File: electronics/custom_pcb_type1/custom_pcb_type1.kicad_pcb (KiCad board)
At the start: 2 copper layers, 124.5 x 81.3 mm, 25 parts, among them J1 BELT_CONN_1, J2 BELT_CONN_2, J3 SEN0140, J4 USB_B, J5 JMPR_TO_ATMEGA, Q1 2N2222, Q2 2N2222, Q3 2N2222, Q4 2N2222, Q5 2N2222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

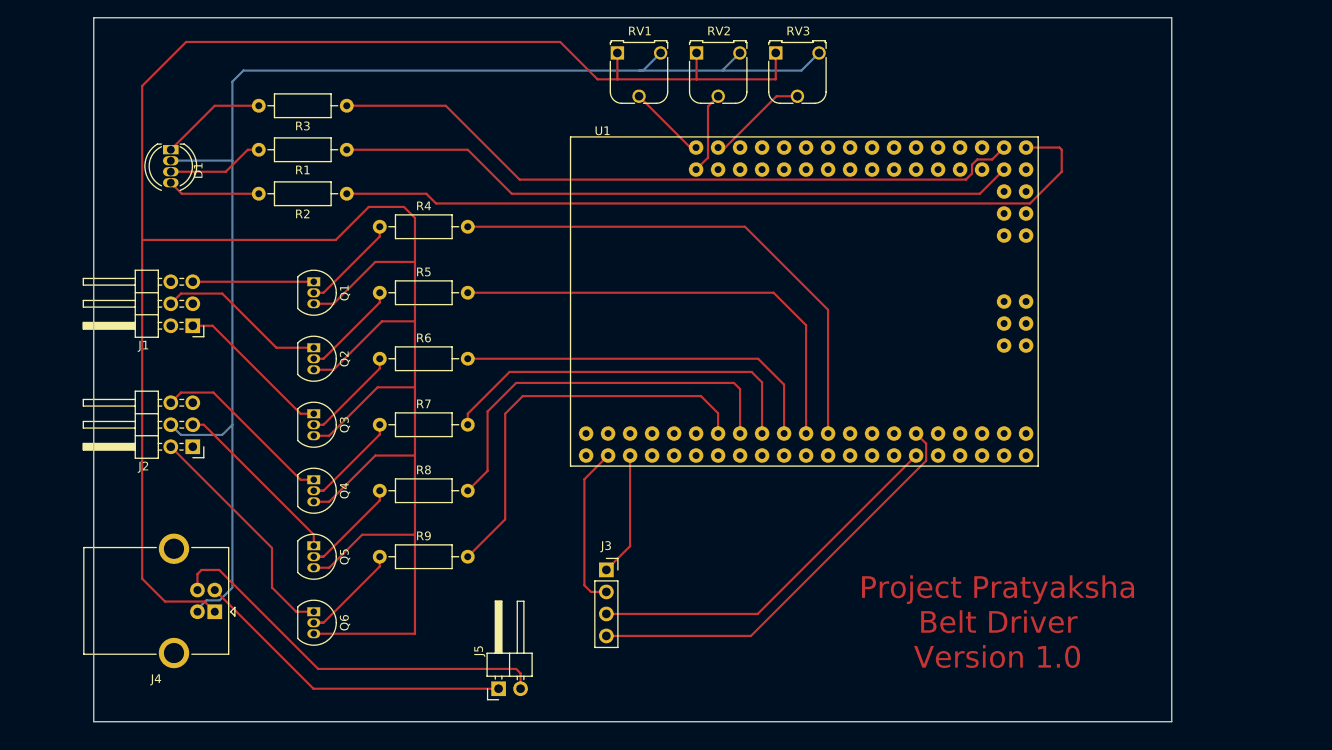
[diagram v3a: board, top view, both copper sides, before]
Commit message: Size matters
Welp Got all the way to putting the transfer paper onto the PCB when I found out that my raw PCBs are kinda small. 70mm x 100mm - which is a lot smaller than the current footprint of like 90mm x 120mm. So LOTS of rearranging things and reassigning pins. I think the end result is a far better board than the previous one so It was well worth the effort. I made sure to not route any traces too close to the edge, other traces, or other pin holes. Trying to give the toner transfer the best possible chance of at least not bridging stuff.
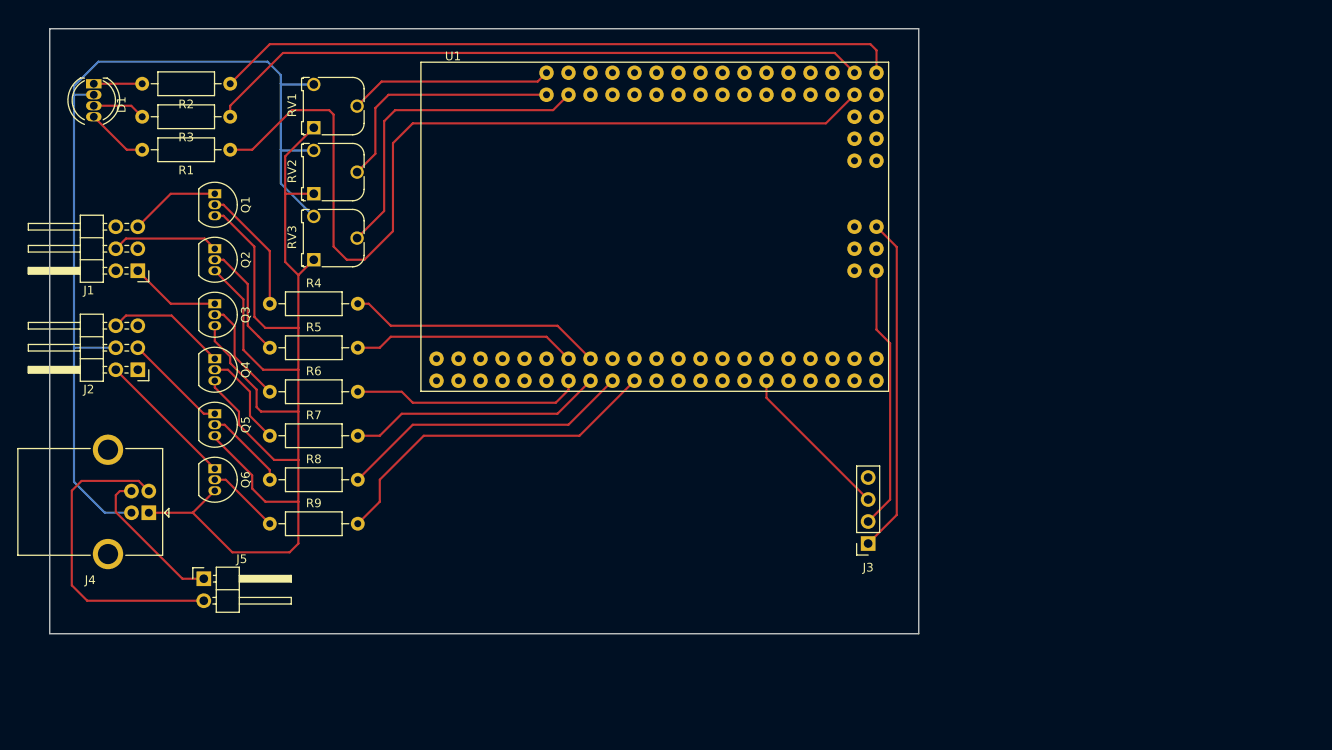
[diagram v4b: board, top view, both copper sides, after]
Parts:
- moved RV3 58.4 mm to (94.0, 94.0), turned to 90 degrees
- moved RV2 47.1 mm to (94.0, 86.4), turned to 90 degrees
- moved J5 36.3 mm to (81.3, 130.8), turned to 0 degrees
- moved RV1 36.1 mm to (94.0, 78.7), turned to 90 degrees
- moved J3 30.4 mm to (158.0, 126.7), turned to 180 degrees
- moved Q6 20.1 mm to (82.5, 118.1)
- moved U1 19.3 mm to (133.3, 90.2)
- moved Q5 19.1 mm to (82.5, 111.8)
- moved R2 18.5 mm to (84.3, 73.7)
- moved Q4 18.1 mm to (82.5, 105.4)
- moved Q3 17.1 mm to (82.5, 99.1)
- moved Q2 16.2 mm to (82.5, 92.7)
- moved R4 15.5 mm to (88.9, 99.1)
- moved Q1 15.3 mm to (82.5, 86.4)
- moved R5 14.2 mm to (88.9, 104.1)
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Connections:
- J5 pad 1: Net-(J4-Pad2) -> Net-(J4-Pad3)
- J5 pad 2: Net-(J4-Pad3) -> Net-(J4-Pad2)
- R1 pad 2: Net-(D1-Pad3) -> Net-(D1-Pad4)
- R2 pad 2: Net-(D1-Pad4) -> Net-(D1-Pad1)
- R3 pad 2: Net-(D1-Pad1) -> Net-(D1-Pad3)
- U1 pad A2: Net-(RV3-Pad2) -> Net-(U1-PadA2)
- U1 pad A3: Net-(U1-PadA3) -> Net-(RV3-Pad2)
- U1 pad D10: Net-(R5-Pad2) -> Net-(U1-PadD10)
- U1 pad D12: Net-(R4-Pad2) -> Net-(U1-PadD12)
- U1 pad D2: Net-(R9-Pad2) -> Net-(R5-Pad2)
- U1 pad D3: Net-(U1-PadD3) -> Net-(R6-Pad2)
- U1 pad D4: Net-(R8-Pad2) -> Net-(R4-Pad2)
- U1 pad D5: Net-(U1-PadD5) -> Net-(R7-Pad2)
- U1 pad D6: Net-(R7-Pad2) -> Net-(U1-PadD6)
- U1 pad D7: Net-(U1-PadD7) -> Net-(R8-Pad2)
- U1 pad D8: Net-(R6-Pad2) -> Net-(U1-PadD8)
- U1 pad D9: Net-(U1-PadD9) -> Net-(R9-Pad2)
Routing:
- net +5V: track 315.2 -> 161.6 mm
- net Net-(J3-Pad4): track 48.9 -> 0.00 mm
- net GND: track 154.2 -> 112.2 mm
- net Net-(R4-Pad2): track 59.9 -> 29.5 mm
- net Net-(J4-Pad3): track 46.1 -> 17.3 mm
- net Net-(R5-Pad2): track 53.1 -> 25.9 mm
- net Net-(RV3-Pad2): track 11.6 -> 37.3 mm
- net Net-(J3-Pad3): track 43.3 -> 18.6 mm
- net Net-(R1-Pad1): track 79.2 -> 103.9 mm
- net Net-(J3-Pad1): track 15.2 -> 38.9 mm
- net Net-(RV2-Pad2): track 9.52 -> 28.7 mm
- net Net-(R6-Pad2): track 43.4 -> 26.5 mm
- net Net-(RV1-Pad2): track 9.04 -> 23.5 mm
- net Net-(R7-Pad2): track 43.7 -> 29.5 mm
- net Net-(R8-Pad2): track 46.0 -> 34.1 mm
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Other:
- board size 124.5 x 81.3 mm -> 100.3 x 69.8 mm
- board text removed: "Project Pratyaksha Belt Driver Version 1.0"

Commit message: Forgot some text
Forgot the text I added to identify the board and version. It should be nicely visible even after all components are on the board.
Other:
- board text added: "Project Pratyaksha Belt Driver Version 1.0"
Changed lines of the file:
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@@
   (general
     (thickness 1.6)
-    (drawings 9)
+    (drawings 10)
     (tracks 178)
     (zones 0)
@@
   (layers
     (0 F.Cu signal)
-    (31 B.Cu signal hide)
+    (31 B.Cu signal)
     (33 F.Adhes user)
     (35 F.Paste user)
@@
     (43 Eco2.User user)
     (44 Edge.Cuts user)
-    (45 Margin user hide)
+    (45 Margin user)
     (46 B.CrtYd user)
     (47 F.CrtYd user)
@@
     )
   )
+  (gr_text "Project Pratyaksha\nBelt Driver\nVersion 1.0" (at 113.792 127.762 180) (layer F.Cu)
+    (effects (font (size 2.5 2.5) (thickness 0.3)))
+  )
   (gr_line (start 163.83 67.31) (end 163.83 137.16) (layer Edge.Cuts) (width 0.1))

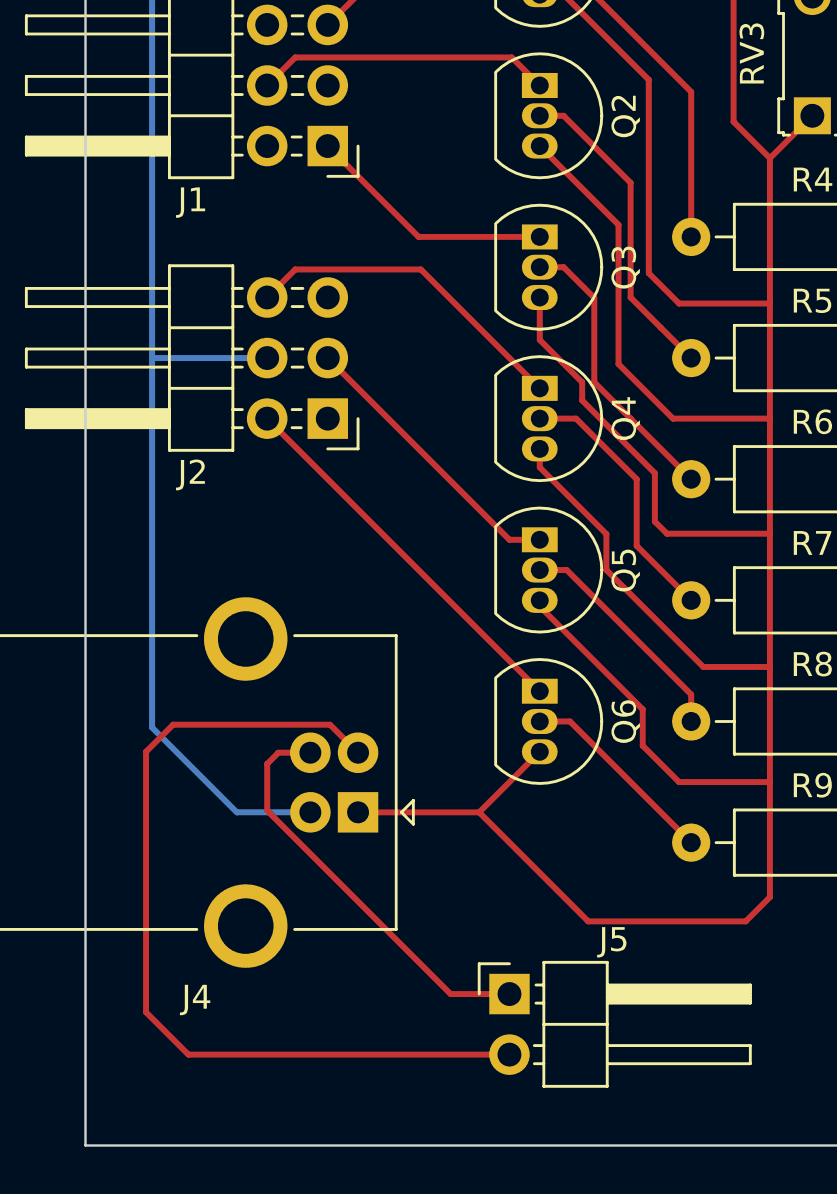
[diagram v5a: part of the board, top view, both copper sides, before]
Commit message: Moved some traces
Finally got around to trying to make the PCB and it actually went fairly well. My first try had something mostly workable, just a few traces that bridged here and there. Probably just improper technique but I decided to rearrange those traces to have more space around them anyway. Now even if I mess up the transfer hopefully the extra space saves me.

With this first board I was only interested in the processes and not the final product so I didnt attempt to protect the back from etching. I realized theres only like 4 or 5 ground connections anyway so I can just manually wire that up. I discovered by accident that the PTFE fiberglass high-temp tape I have protects the copper perfectly after its been ironed on (not sure if heat is necessary though). The idea is to just replicate the process again but instead of removing the tape just leave it on to etch the one side only. Then do the other side the same way.

Anyway onto drilling this board and seeing if I can actually use it. Next board will be printed with the corrected layout. Also need to add drill hole markers for the PCB mounting holes. Totally forgot about that.
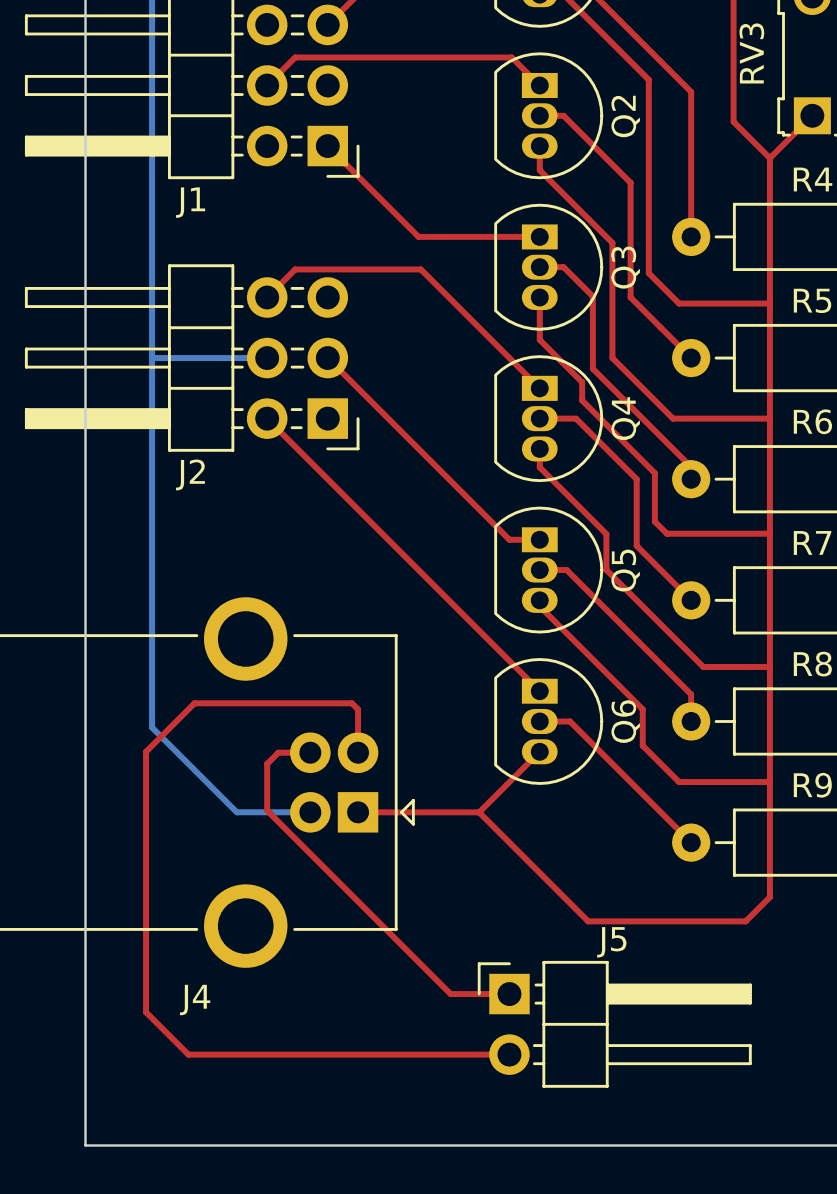
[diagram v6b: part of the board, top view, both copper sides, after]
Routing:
- net Net-(J4-Pad2): track 36.7 -> 38.6 mm
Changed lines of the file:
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@@
-(kicad_pcb (version 20171130) (host pcbnew "(5.1.10)-1")
+(kicad_pcb (version 20171130) (host pcbnew "(5.1.9)-1")
   (general
     (thickness 1.6)
     (drawings 10)
-    (tracks 178)
+    (tracks 180)
     (zones 0)
     (modules 25)
@@
       (effects (font (size 1 1) (thickness 0.15)))
     )
-    (fp_text user %R (at 2.77 1.27 90) (layer F.Fab)
-      (effects (font (size 1 1) (thickness 0.15)))
-    )
     (fp_line (start 2.135 -1.27) (end 4.04 -1.27) (layer F.Fab) (width 0.1))
     (fp_line (start 4.04 -1.27) (end 4.04 3.81) (layer F.Fab) (width 0.1))
@@
     (fp_line (start 10.55 4.35) (end 10.55 -1.8) (layer F.CrtYd) (width 0.05))
     (fp_line (start 10.55 -1.8) (end -1.8 -1.8) (layer F.CrtYd) (width 0.05))
+    (fp_text user %R (at 2.77 1.27 90) (layer F.Fab)
+      (effects (font (size 1 1) (thickness 0.15)))
+    )
     (pad 1 thru_hole rect (at 0 0) (size 1.7 1.7) (drill 1) (layers *.Cu *.Mask)
       (net 19 "Net-(J4-Pad3)"))
@@
   (segment (start 92.202 101.854) (end 92.202 95.758) (width 0.25) (layer F.Cu) (net 17))
   (segment (start 87.122 100.584) (end 88.392 101.854) (width 0.25) (layer F.Cu) (net 17))
-  (segment (start 82.55 95.25) (end 85.852 98.552) (width 0.25) (layer F.Cu) (net 17))
-  (segment (start 85.852 98.552) (end 85.852 104.394) (width 0.25) (layer F.Cu) (net 17))
-  (segment (start 85.852 104.394) (end 88.138 106.68) (width 0.25) (layer F.Cu) (net 17))
-  (segment (start 88.138 106.68) (end 92.202 106.68) (width 0.25) (layer F.Cu) (net 17))
   (segment (start 92.202 106.68) (end 92.202 101.854) (width 0.25) (layer F.Cu) (net 17))
   (segment (start 82.55 101.6) (end 82.55 103.378) (width 0.25) (layer F.Cu) (net 17))
@@
   (segment (start 92.202 121.92) (end 92.202 117.094) (width 0.25) (layer F.Cu) (net 17))
   (segment (start 92.202 126.746) (end 92.202 121.92) (width 0.25) (layer F.Cu) (net 17))
+  (segment (start 88.138 106.68) (end 92.202 106.68) (width 0.25) (layer F.Cu) (net 17))
+  (segment (start 85.598 104.14) (end 88.138 106.68) (width 0.25) (layer F.Cu) (net 17))
+  (segment (start 85.598 99.314) (end 85.598 104.14) (width 0.25) (layer F.Cu) (net 17))
+  (segment (start 82.55 96.266) (end 85.598 99.314) (width 0.25) (layer F.Cu) (net 17))
+  (segment (start 82.55 95.25) (end 82.55 96.266) (width 0.25) (layer F.Cu) (net 17))
   (segment (start 72.93 120.69) (end 71.588 120.69) (width 0.25) (layer F.Cu) (net 19))
   (segment (start 71.588 120.69) (end 71.12 121.158) (width 0.25) (layer F.Cu) (net 19))
@@
   (segment (start 71.12 123.119002) (end 78.810998 130.81) (width 0.25) (layer F.Cu) (net 19))
   (segment (start 71.12 121.158) (end 71.12 123.119002) (width 0.25) (layer F.Cu) (net 19))
-  (segment (start 73.754999 119.514999) (end 74.93 120.69) (width 0.25) (layer F.Cu) (net 20))
-  (segment (start 67.175001 119.514999) (end 73.754999 119.514999) (width 0.25) (layer F.Cu) (net 20))
-  (segment (start 66.04 131.572) (end 66.04 120.65) (width 0.25) (layer F.Cu) (net 20))
-  (segment (start 67.818 133.35) (end 66.04 131.572) (width 0.25) (layer F.Cu) (net 20))
-  (segment (start 66.04 120.65) (end 67.175001 119.514999) (width 0.25) (layer F.Cu) (net 20))
-  (segment (start 81.28 133.35) (end 67.818 133.35) (width 0.25) (layer F.Cu) (net 20))
+  (segment (start 66.04 131.572) (end 67.818 133.35) (width 0.25) (layer F.Cu) (net 20))
+  (segment (start 67.818 133.35) (end 81.28 133.35) (width 0.25) (layer F.Cu) (net 20))
+  (segment (start 66.04 120.65) (end 66.04 131.572) (width 0.25) (layer F.Cu) (net 20))
+  (segment (start 68.072 118.618) (end 66.04 120.65) (width 0.25) (layer F.Cu) (net 20))
+  (segment (start 74.676 118.618) (end 68.072 118.618) (width 0.25) (layer F.Cu) (net 20))
+  (segment (start 74.93 118.872) (end 74.676 118.618) (width 0.25) (layer F.Cu) (net 20))
+  (segment (start 74.93 120.69) (end 74.93 118.872) (width 0.25) (layer F.Cu) (net 20))
   (segment (start 83.55 87.63) (end 82.55 87.63) (width 0.25) (layer F.Cu) (net 21))
   (segment (start 88.9 92.98) (end 83.55 87.63) (width 0.25) (layer F.Cu) (net 21))
@@
   (segment (start 86.36 101.6) (end 87.63 102.87) (width 0.25) (layer F.Cu) (net 22))
   (segment (start 86.36 96.79) (end 86.36 101.6) (width 0.25) (layer F.Cu) (net 22))
-  (segment (start 88.9 109.22) (end 86.36 106.68) (width 0.25) (layer F.Cu) (net 23))
-  (segment (start 83.55 100.33) (end 84.836 101.616) (width 0.25) (layer F.Cu) (net 23))
+  (segment (start 88.9 108.712) (end 88.9 109.22) (width 0.25) (layer F.Cu) (net 23))
+  (segment (start 84.778009 104.590009) (end 88.9 108.712) (width 0.25) (layer F.Cu) (net 23))
+  (segment (start 84.778009 101.558009) (end 84.778009 104.590009) (width 0.25) (layer F.Cu) (net 23))
+  (segment (start 83.55 100.33) (end 84.778009 101.558009) (width 0.25) (layer F.Cu) (net 23))
   (segment (start 82.55 100.33) (end 83.55 100.33) (width 0.25) (layer F.Cu) (net 23))
-  (segment (start 84.836 105.156) (end 86.36 106.68) (width 0.25) (layer F.Cu) (net 23))
-  (segment (start 84.836 101.616) (end 84.836 105.156) (width 0.25) (layer F.Cu) (net 23))
   (segment (start 82.55 106.68) (end 84.074 106.68) (width 0.25) (layer F.Cu) (net 24))
   (segment (start 84.074 106.68) (end 86.614 109.22) (width 0.25) (layer F.Cu) (net 24))

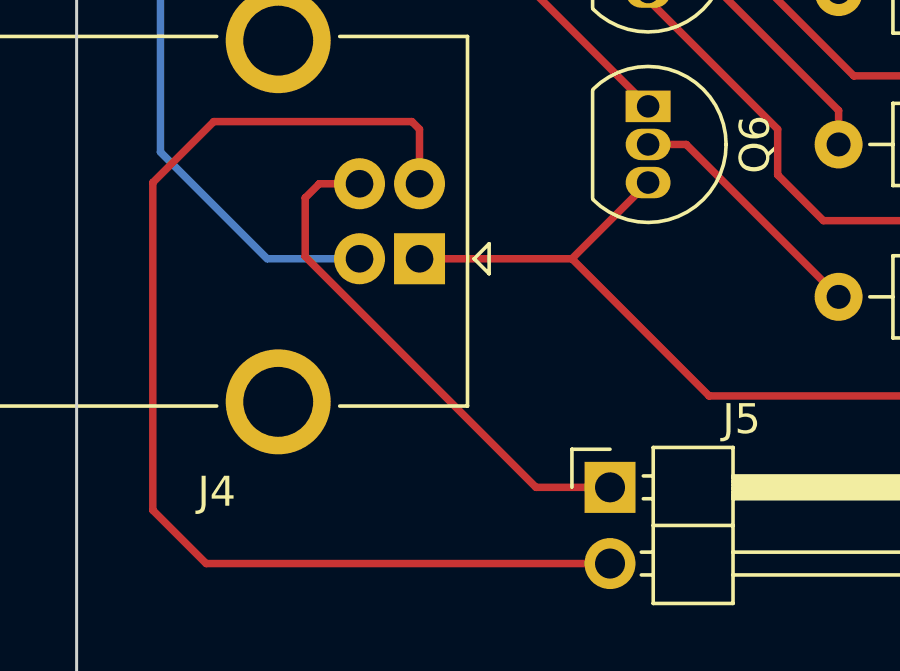
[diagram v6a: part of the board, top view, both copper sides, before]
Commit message: D+ trace move
D+ ran a bit close to the GND pad of the USB connector. It didnt bridge in my first PCB but Its easy enough to move a little and avoid any problems in the future.
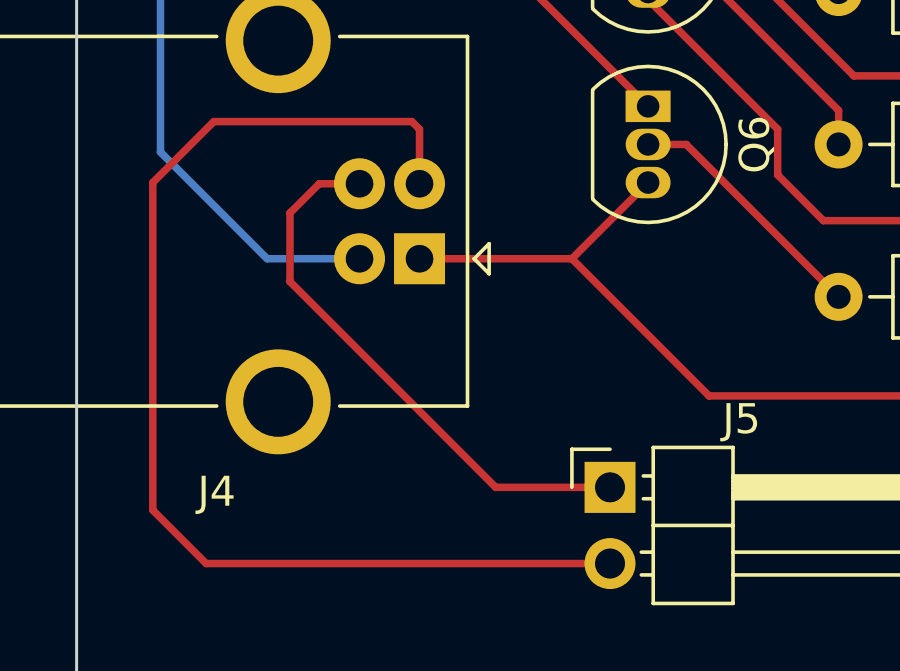
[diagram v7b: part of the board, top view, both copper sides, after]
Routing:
- net Net-(J4-Pad3): track 17.3 -> 18.5 mm
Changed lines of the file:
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@@
   (segment (start 82.55 96.266) (end 85.598 99.314) (width 0.25) (layer F.Cu) (net 17))
   (segment (start 82.55 95.25) (end 82.55 96.266) (width 0.25) (layer F.Cu) (net 17))
-  (segment (start 72.93 120.69) (end 71.588 120.69) (width 0.25) (layer F.Cu) (net 19))
-  (segment (start 71.588 120.69) (end 71.12 121.158) (width 0.25) (layer F.Cu) (net 19))
-  (segment (start 78.810998 130.81) (end 81.28 130.81) (width 0.25) (layer F.Cu) (net 19))
-  (segment (start 71.12 123.119002) (end 78.810998 130.81) (width 0.25) (layer F.Cu) (net 19))
-  (segment (start 71.12 121.158) (end 71.12 123.119002) (width 0.25) (layer F.Cu) (net 19))
+  (segment (start 71.588 120.69) (end 72.93 120.69) (width 0.25) (layer F.Cu) (net 19))
+  (segment (start 70.612 123.952) (end 70.612 121.666) (width 0.25) (layer F.Cu) (net 19))
+  (segment (start 77.47 130.81) (end 70.612 123.952) (width 0.25) (layer F.Cu) (net 19))
+  (segment (start 70.612 121.666) (end 71.588 120.69) (width 0.25) (layer F.Cu) (net 19))
+  (segment (start 81.28 130.81) (end 77.47 130.81) (width 0.25) (layer F.Cu) (net 19))
   (segment (start 66.04 131.572) (end 67.818 133.35) (width 0.25) (layer F.Cu) (net 20))
   (segment (start 67.818 133.35) (end 81.28 133.35) (width 0.25) (layer F.Cu) (net 20))
